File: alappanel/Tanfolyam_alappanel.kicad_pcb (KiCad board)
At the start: 2 copper layers, 70.7 x 41.1 mm, 35 parts, among them J1 Connector, J2 Connector, J3 Connector, SW1 SW_Push, SW2 SW_Push, U1 74HC595, U2 74HC595, U3 SA39-11SRWA, U4 SA39-11SRWA

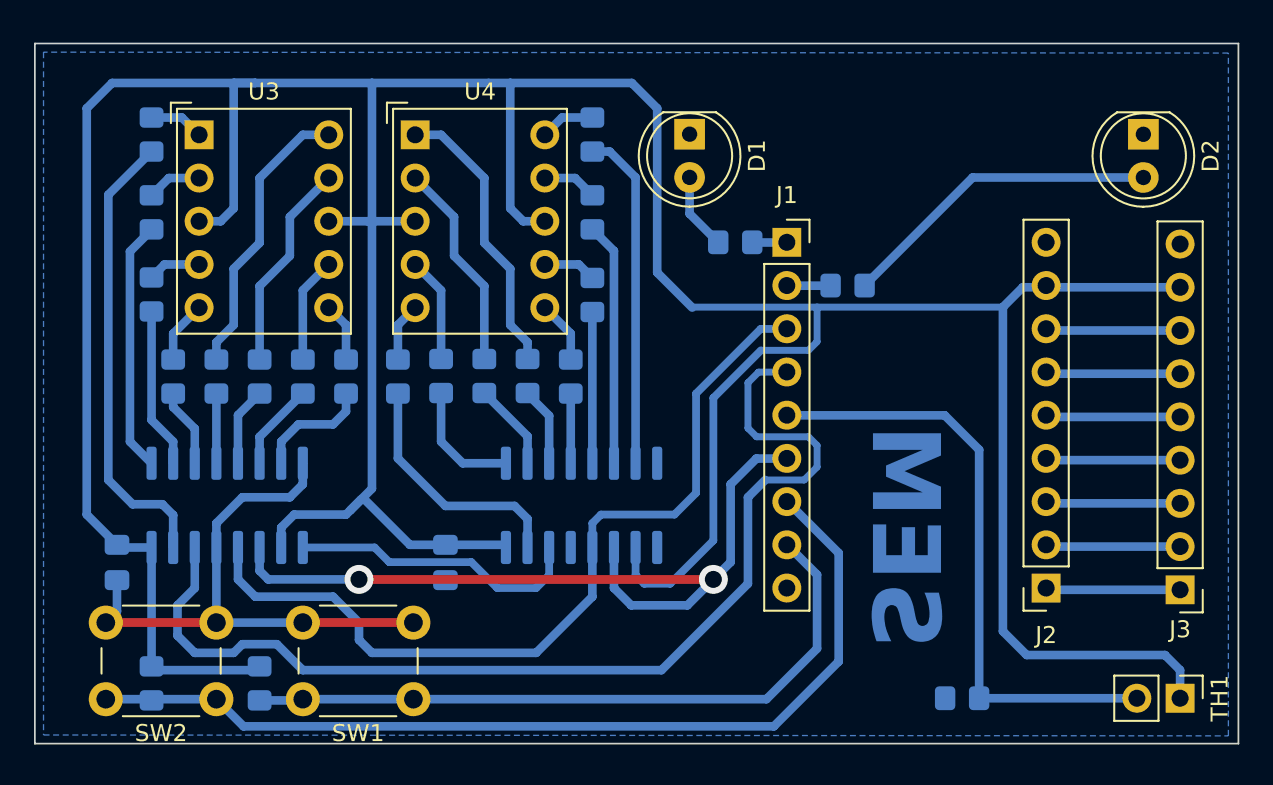
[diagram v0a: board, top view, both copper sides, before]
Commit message: Changed 0805 footprints to 1206
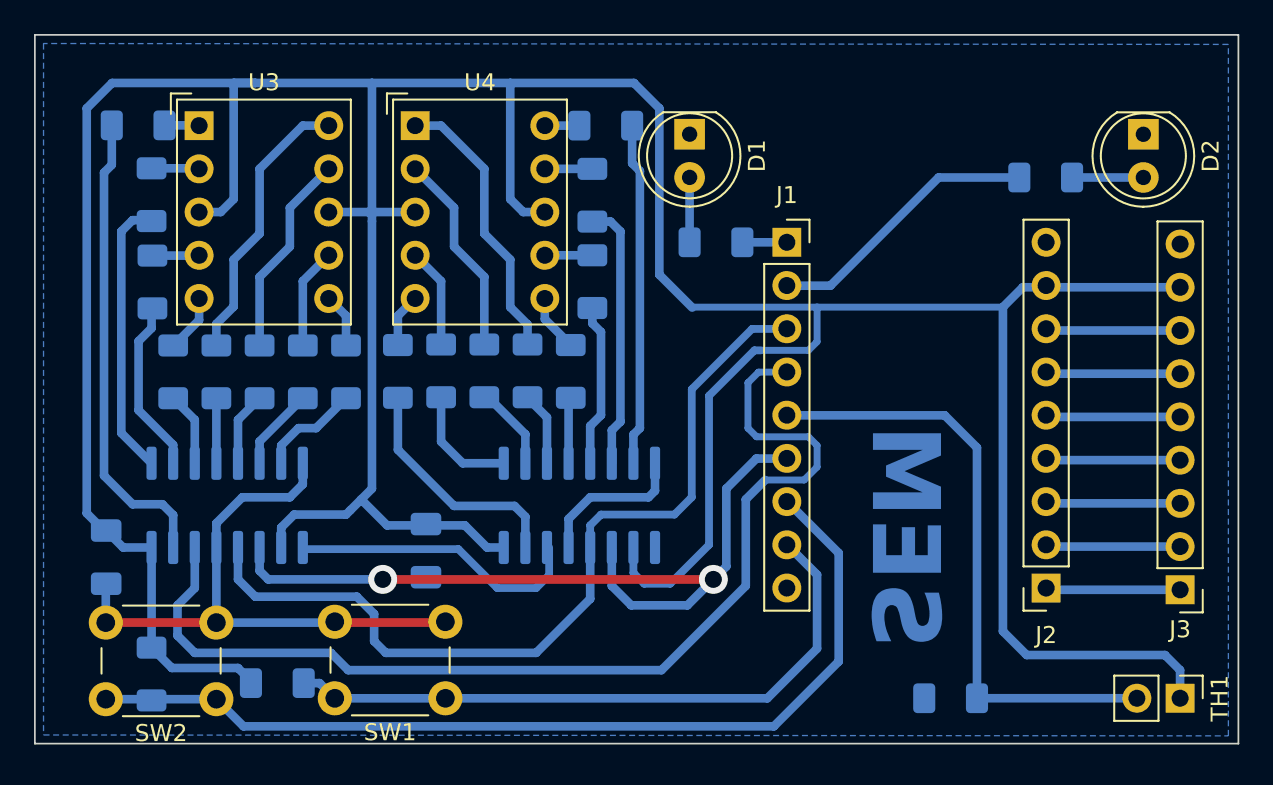
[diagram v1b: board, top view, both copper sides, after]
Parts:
- C1, C2: footprint Capacitor_SMD:C_0805_2012Metric_Pad1.18x1.45mm_HandSolder -> Capacitor_SMD:C_1206_3216Metric_Pad1.33x1.80mm_HandSolder
- R1, R10, R11, R12, R13, R14, R15, R16, R17, R18, R19, R2, R20, R21, R3, R4, R5, R6, R7, R8, R9: footprint Resistor_SMD:R_0805_2012Metric_Pad1.20x1.40mm_HandSolder -> Resistor_SMD:R_1206_3216Metric_Pad1.30x1.75mm_HandSolder
- moved R5 13.3 mm to (162.5, 83.3)
- moved SW1 1.88 mm to (127.3, 113.9)
- moved C2 1.34 mm to (126.1, 105.2)
- moved R4 1.13 mm to (143.2, 87.1)
- moved R2 1.04 mm to (117.4, 113.0), turned to 0 degrees
- moved R11 1.04 mm to (110.0, 84.3)
- moved R15 1.01 mm to (135.9, 84.4)
- moved R12 0.96 mm to (109.2, 80.2), turned to 0 degrees
- moved R14 0.95 mm to (136.7, 80.3), turned to 180 degrees
- moved R16 0.78 mm to (135.9, 89.4)
- moved R10 0.73 mm to (110.0, 89.5)
- moved C1 0.71 mm to (107.3, 105.6)
- moved R1 0.68 mm to (156.9, 113.9)
- moved R3 0.55 mm to (110.0, 112.5)
- moved U3 0.54 mm to (112.8, 80.3)
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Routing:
- net Net-(D2-A): track 19.0 -> 4.19 mm
- net /P1.1: track 2.56 -> 16.3 mm
- net GND: track 34.3 -> 44.0 mm
- net VCC: track 243.3 -> 240.5 mm
- net Net-(U1-QB): track 14.8 -> 16.4 mm
- net Net-(U2-QG): track 14.3 -> 15.7 mm
- net /P1.7: track 39.8 -> 38.6 mm
- net Net-(U4-A): track 3.21 -> 2.03 mm
- net Net-(U3-G): track 3.21 -> 2.04 mm
- net Net-(U1-QC): track 9.45 -> 10.6 mm
- net Net-(U1-QH): track 6.86 -> 6.01 mm
- net Net-(U1-QE): track 4.10 -> 3.28 mm
- net Net-(U1-QA): track 26.9 -> 27.7 mm
- net Net-(U2-QA): track 14.6 -> 13.9 mm
- net /P1.2: track 50.4 -> 51.0 mm
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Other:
- board size 70.7 x 41.1 mm -> 70.7 x 41.7 mm

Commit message: Gyártva a SEM-ben.
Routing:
- net Net-(U1-QH): track 6.01 -> 6.59 mm

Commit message: Add 7-segment display 3D model and tutorial (demo) project for kicad8
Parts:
- moved R2 0.89 mm to (117.4, 113.9)
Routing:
- net VCC: track 240.5 -> 241.7 mm
